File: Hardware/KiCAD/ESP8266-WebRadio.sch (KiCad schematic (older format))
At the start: 51 parts

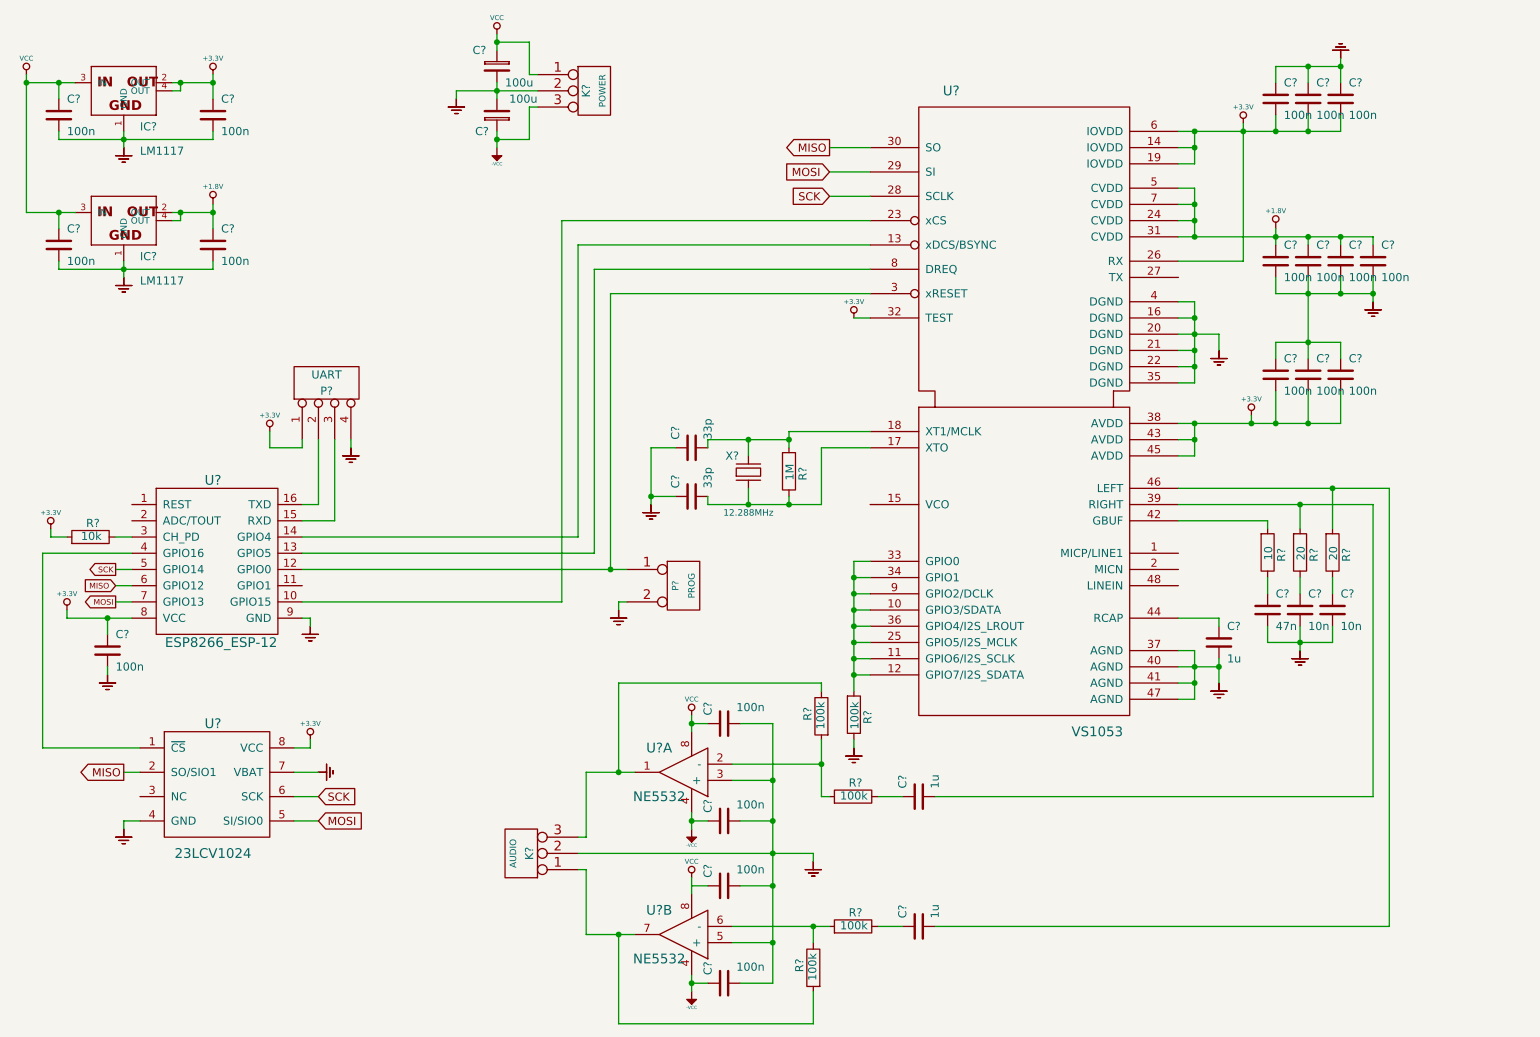
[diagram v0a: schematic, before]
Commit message: Added schematic and PCB of main board
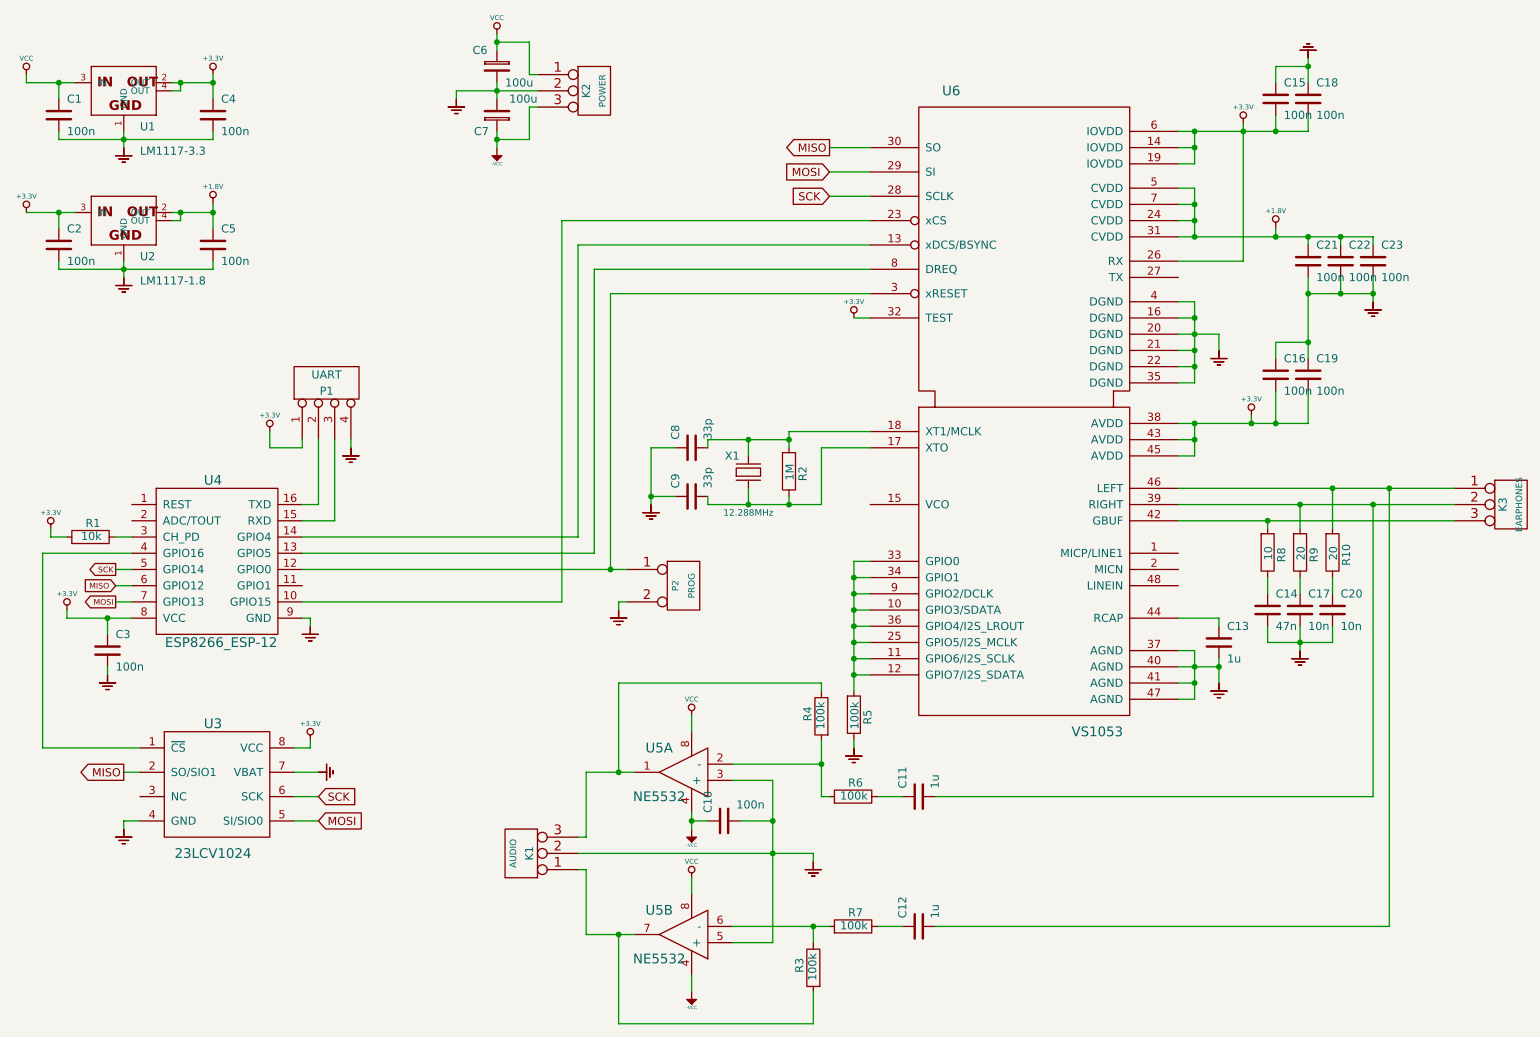
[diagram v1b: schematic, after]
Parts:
- removed C? (x6): 100n, symbol C
- added K3: EARPHONES, symbol CONN_3
- U1: renamed from IC?; value LM1117 -> LM1117-3.3
- U2: renamed from IC?; value LM1117 -> LM1117-1.8
- gave numbers to parts that had none: 42
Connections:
- net +1.8V: now also C21.1
- net +3.3V: now also C2.1, U2.3 (IN); no longer C21.2
- net GND: now also C21.2; no longer C21.1
- net VCC: no longer C2.1, U2.3 (IN)
- net at C11.2, R9.1, U6.39 (RIGHT): now also K3.2 (PM)
- net at R8.1, U6.42 (GBUF): now also K3.3 (P3)
- net at C12.2, R10.1, U6.46 (LEFT): now also K3.1 (P1)
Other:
- moved on the sheet: C21
